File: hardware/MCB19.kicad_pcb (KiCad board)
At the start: 2 copper layers, 172.8 x 81.5 mm, 137 parts, among them J401 USART, J402 DISABLE, J601 RJ45, J602 RJ45, J611 +BAT_IN, J612 -BAT_IN, J613 +BAT_OUT, J614 -BAT_OUT, K601 G5LE-1, Q601 IRFP260N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

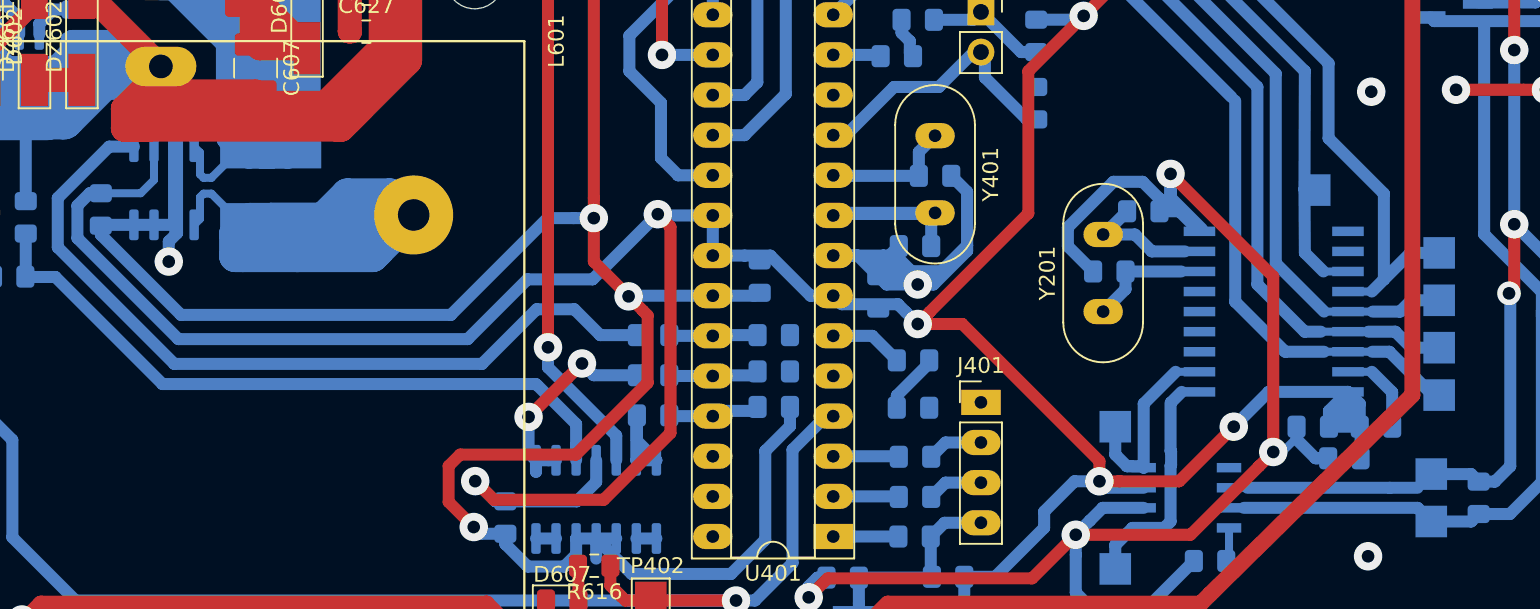
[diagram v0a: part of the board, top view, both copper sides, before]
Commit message: some necks removed
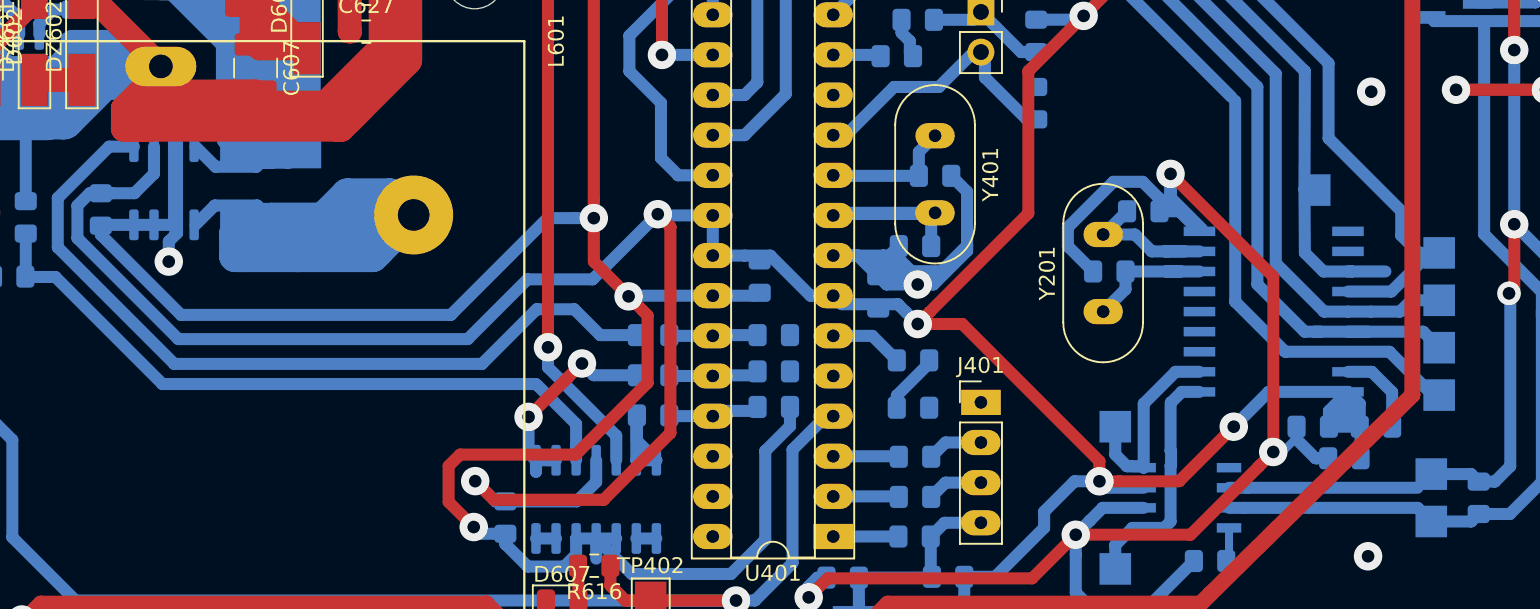
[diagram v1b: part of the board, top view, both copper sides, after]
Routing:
- net /MISO: track 72.3 -> 77.0 mm
- net /CANBUS/INT: track 60.9 -> 63.3 mm
- net Net-(C204-Pad1): track 8.66 -> 10.9 mm
- net Net-(C203-Pad1): track 7.81 -> 9.91 mm
- net Net-(L601-Pad1): track 64.2 -> 62.7 mm
- net Net-(C601-Pad2): track 256.2 -> 254.7 mm
- net /SCK: track 87.3 -> 87.8 mm
